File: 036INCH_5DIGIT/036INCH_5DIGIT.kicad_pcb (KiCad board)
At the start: 2 copper layers, 43.8 x 21 mm, 10 parts, among them J1 Conn_01x04_Female, J2 Conn_01x04_Male, U1 BA56-12SRWA, U2 TM1637

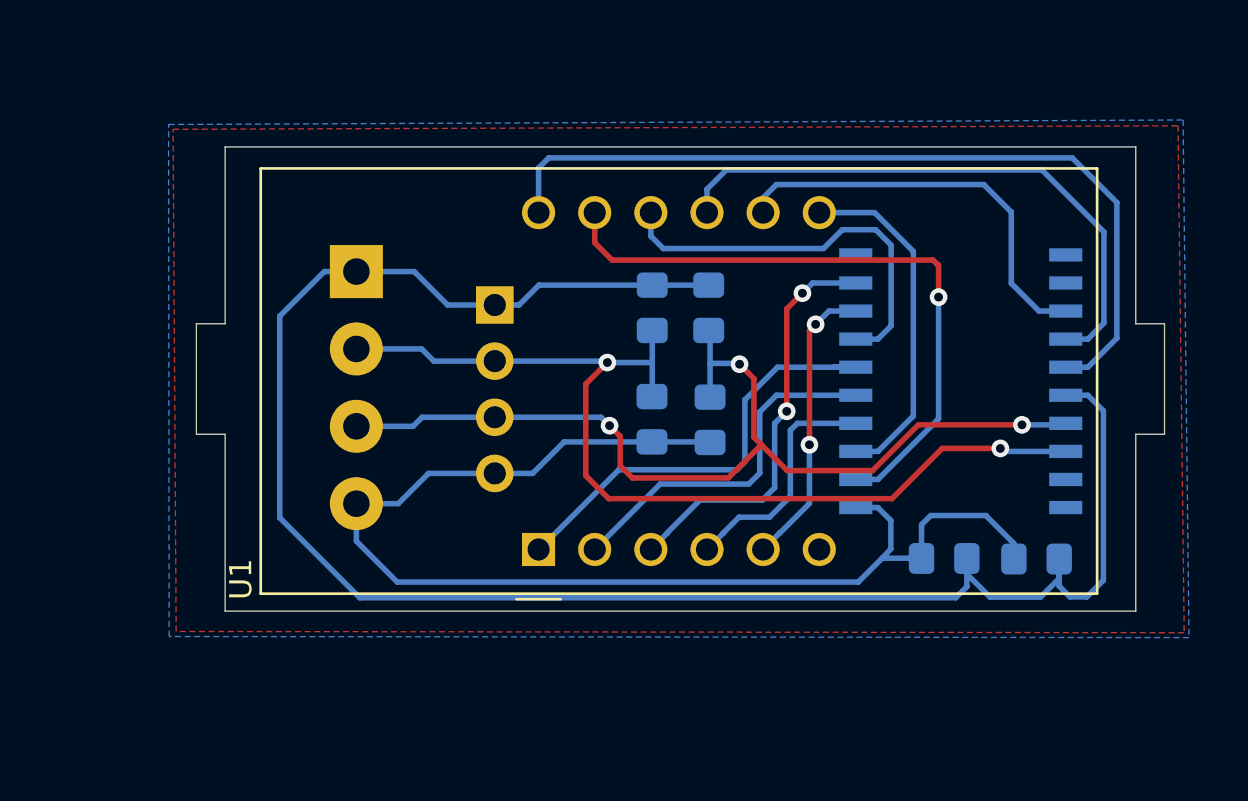
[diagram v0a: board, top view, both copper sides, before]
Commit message: starting placing elements in pcb
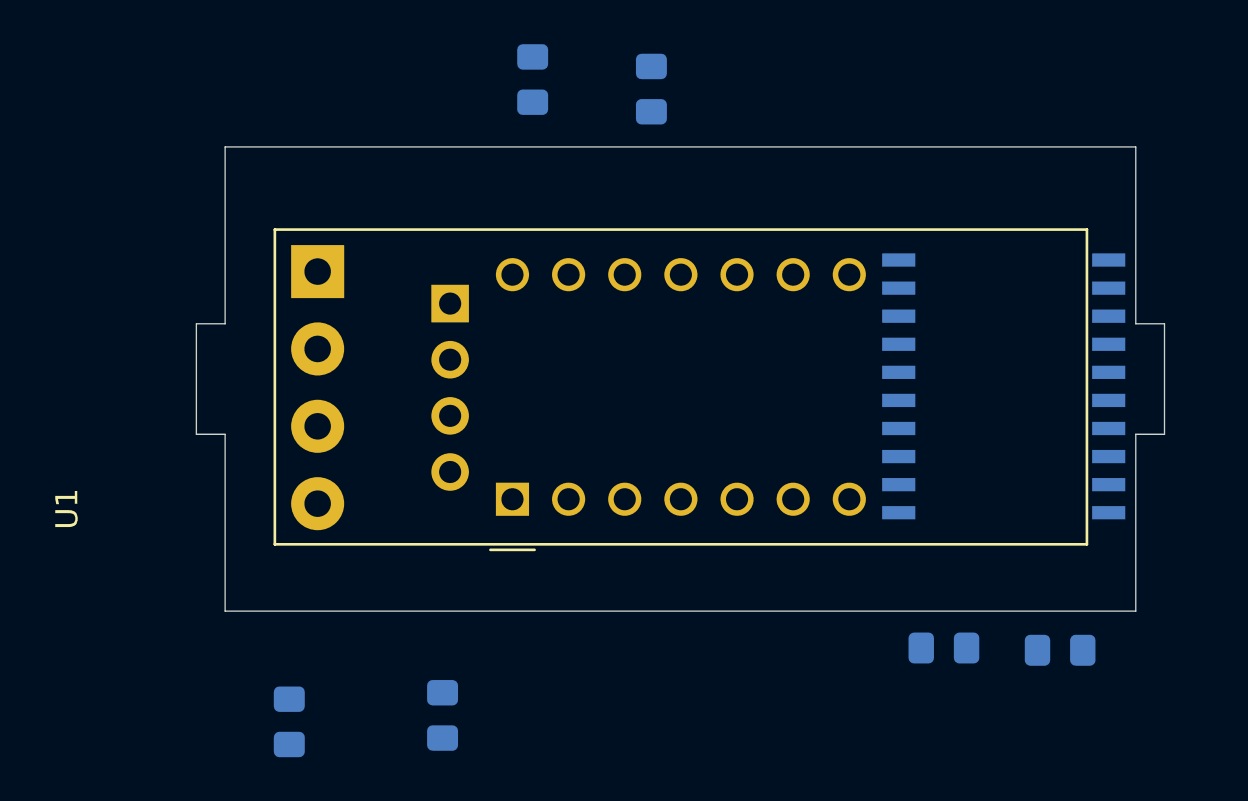
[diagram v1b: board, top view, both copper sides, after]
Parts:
- U1: value BA56-12SRWA -> JM-S03651BH; footprint KINGBRIGHTUSA:BA56-12SRWA -> JINGMEI:JM-S03651BH
- moved C3 21.4 mm to (104.2, 126.0)
- moved C4 18.0 mm to (111.1, 125.7)
- moved R1 11.7 mm to (115.2, 97.0)
- moved R2 10.2 mm to (120.6, 97.4)
- moved C1 4.26 mm to (139.1, 122.8)
- moved C2 4.05 mm to (133.8, 122.7)
- moved U1 2.56 mm to (114.3, 115.9)
- moved J2 2.02 mm to (111.5, 107.1)
- moved U2 1.96 mm to (136.5, 110.8)
- moved J1 1.75 mm to (105.5, 105.6)
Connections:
- U2 pad 11: Net-(U2-Pad11) -> Net-(U1-Pad8)
- U2 pad 12: Net-(U2-Pad12) -> Net-(U1-Pad6)
- U2 pad 13: Net-(U1-Pad8) -> Net-(U1-Pad10)
- U2 pad 14: Net-(U1-Pad9) -> Net-(U1-Pad11)
- U2 pad 15: Net-(U1-Pad12) -> Net-(U1-Pad14)
- U2 pad 2: Net-(U1-Pad11) -> Net-(U1-Pad13)
- U2 pad 3: Net-(U1-Pad7) -> Net-(U1-Pad9)
- U2 pad 7: Net-(U1-Pad10) -> Net-(U1-Pad12)
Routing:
- net Net-(C1-Pad1): track 84.4 -> 0.00 mm
- net Net-(C1-Pad2): track 56.4 -> 0.00 mm
- net Net-(C3-Pad1): track 45.3 -> 0.00 mm, vias 2 -> 0
- net Net-(C4-Pad1): track 44.6 -> 0.00 mm, vias 3 -> 0
- net Net-(U1-Pad12): track 38.2 -> 0.00 mm
- net Net-(U1-Pad11): track 29.2 -> 0.00 mm, vias 1 -> 0
- net Net-(U1-Pad9): track 26.7 -> 0.00 mm
- net Net-(U1-Pad1): track 20.4 -> 0.00 mm
- net Net-(U1-Pad8): track 18.9 -> 0.00 mm
- net Net-(U1-Pad3): track 18.7 -> 0.00 mm, vias 2 -> 0
- net Net-(U1-Pad10): track 18.3 -> 0.00 mm
- net Net-(U1-Pad2): track 16.3 -> 0.00 mm
- net Net-(U1-Pad7): track 15.7 -> 0.00 mm
- net Net-(U1-Pad5): track 13.2 -> 0.00 mm, vias 2 -> 0
- net Net-(U1-Pad4): track 10.9 -> 0.00 mm
- removed copper zone on B.Cu, net Net-(C1-Pad2)
- removed copper zone on F.Cu, net Net-(C1-Pad2)

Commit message: all traces routed
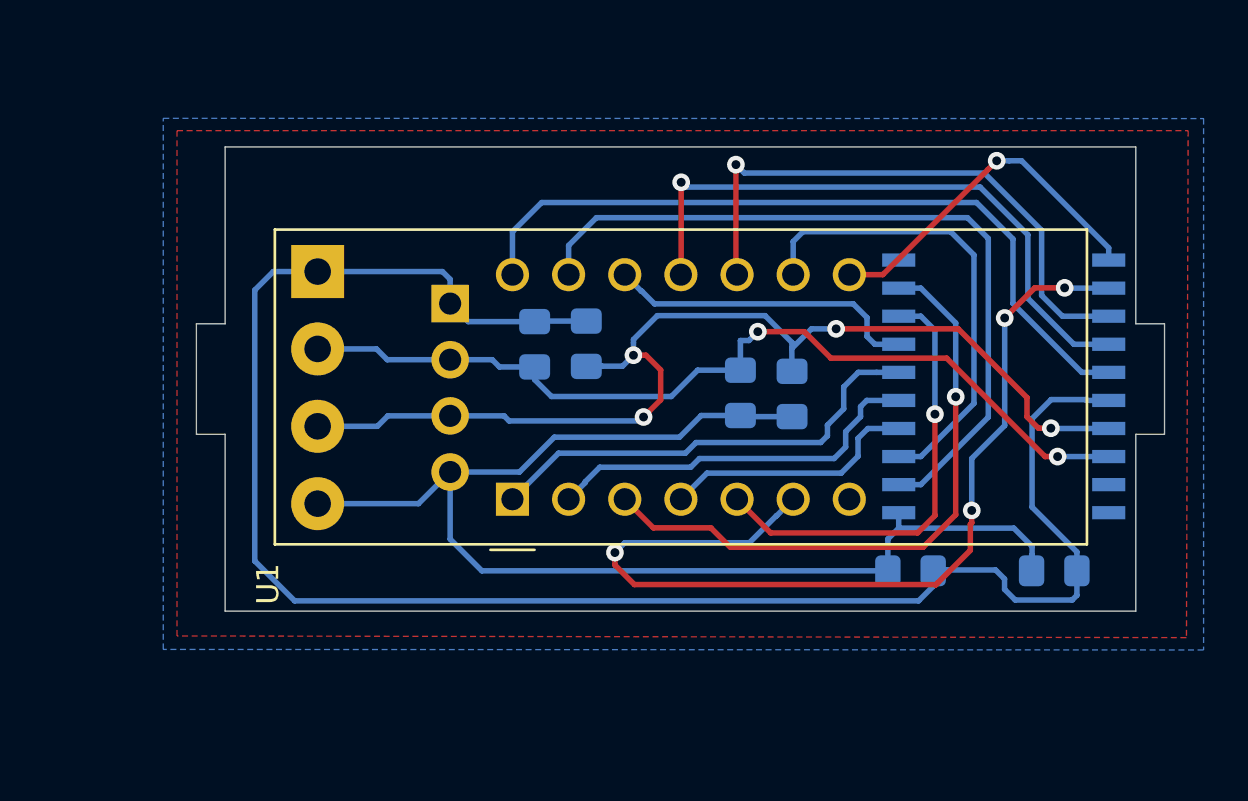
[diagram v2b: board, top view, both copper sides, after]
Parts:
- moved C3 25.3 mm to (124.6, 111.1)
- moved C4 21.5 mm to (126.9, 111.2)
- moved R1 12.0 mm to (115.3, 108.9)
- moved R2 11.9 mm to (117.6, 108.9)
- moved C2 3.81 mm to (132.3, 119.2)
- moved C1 3.60 mm to (138.8, 119.2)
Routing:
- net Net-(C1-Pad1): track 0.00 -> 81.7 mm
- net Net-(C1-Pad2): track 0.00 -> 56.9 mm
- net Net-(C4-Pad1): track 0.00 -> 48.6 mm, vias 0 -> 4
- net Net-(U1-Pad6): track 0.00 -> 43.3 mm, vias 0 -> 4
- net Net-(C3-Pad1): track 0.00 -> 41.4 mm, vias 0 -> 2
- net Net-(U1-Pad13): track 0.00 -> 34.6 mm
- net Net-(U1-Pad14): track 0.00 -> 34.4 mm
- net Net-(U1-Pad3): track 0.00 -> 28.4 mm, vias 0 -> 1
- net Net-(U1-Pad11): track 0.00 -> 28.2 mm, vias 0 -> 1
- net Net-(U1-Pad10): track 0.00 -> 26.4 mm, vias 0 -> 1
- net Net-(U1-Pad9): track 0.00 -> 21.4 mm
- net Net-(U1-Pad1): track 0.00 -> 20.7 mm
- net Net-(U1-Pad5): track 0.00 -> 20.2 mm, vias 0 -> 1
- net Net-(U1-Pad2): track 0.00 -> 17.5 mm
- net Net-(U1-Pad8): track 0.00 -> 16.1 mm, vias 0 -> 1
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- added copper zone on B.Cu, net Net-(C1-Pad2)
- added copper zone on F.Cu, net Net-(C1-Pad2)
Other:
- board text added: "036_5DIG"
- board text removed: "056_3DIG"
